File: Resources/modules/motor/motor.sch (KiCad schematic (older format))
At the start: 15 parts, among them J1 power, J2 from switches, J3 motor, J4 towards uC, U1 L293D

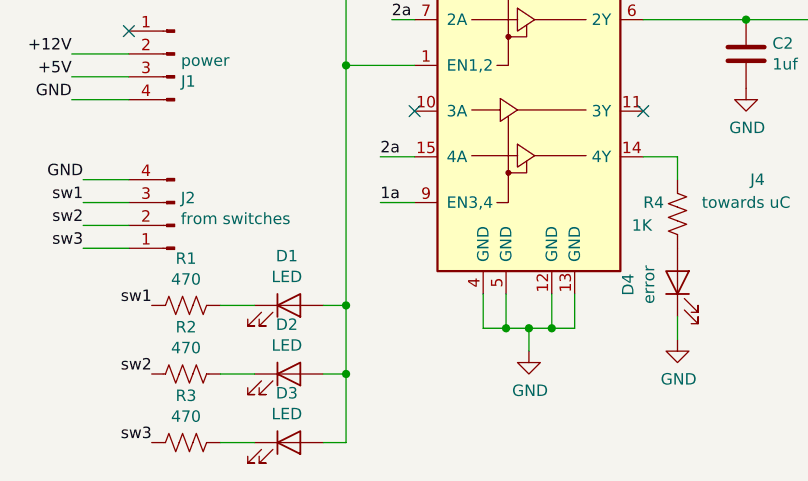
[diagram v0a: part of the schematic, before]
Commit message: Motor module: grounded 'EN3,4'; terminal connector footprint corrected; 'error led' changed to 3mm; proper footprints for 'switches' and 'towards uC' connectors; proper labelling; added 'designed using Kicad' symbol
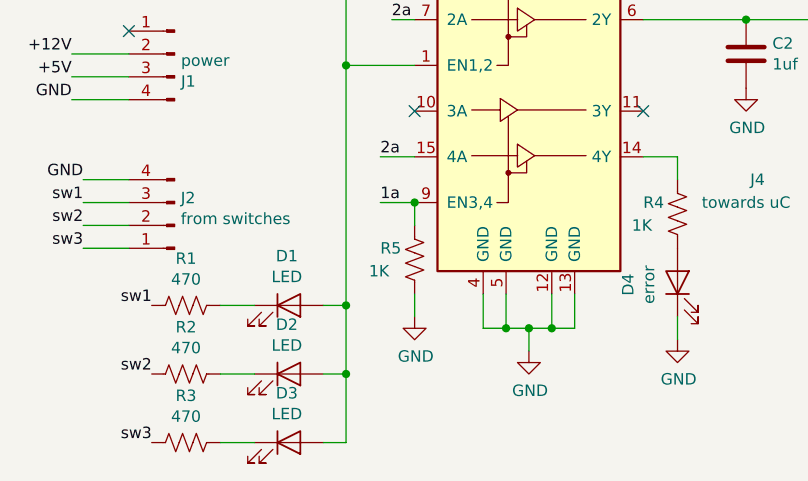
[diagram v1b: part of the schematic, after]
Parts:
- added R5: 1K, Resistor_THT:R_Axial_DIN0207_L6.3mm_D2.5mm_P5.08mm_Vertical, symbol Device:R_US
- C1, C2: footprint Capacitors_THT:C_Disc_D3.8mm_W2.6mm_P2.50mm -> Capacitor_THT:C_Disc_D3.8mm_W2.6mm_P2.50mm
- D1, D2, D3: footprint LEDs:LED_D3.0mm -> LED_THT:LED_D3.0mm
- D4: footprint LEDs:LED_D5.0mm -> LED_THT:LED_D3.0mm
- J1: footprint Connectors_JST:JST_EH_B04B-EH-A_04x2.50mm_Straight -> Connector_JST:JST_EH_B4B-EH-A_1x04_P2.50mm_Vertical
- J2: footprint Connectors_JST:JST_EH_B04B-EH-A_04x2.50mm_Straight -> Connector_PinHeader_2.54mm:PinHeader_1x04_P2.54mm_Vertical
- J3: footprint TerminalBlocks_Phoenix:TerminalBlock_Phoenix_MPT-2.54mm_2pol -> TerminalBlock_Phoenix:TerminalBlock_Phoenix_MKDS-1,5-2_1x02_P5.00mm_Horizontal
- J4: footprint Connectors_JST:JST_EH_B05B-EH-A_05x2.50mm_Straight -> Connector_PinHeader_2.54mm:PinHeader_1x05_P2.54mm_Vertical
- R1, R2, R3, R4: footprint Resistors_THT:R_Axial_DIN0207_L6.3mm_D2.5mm_P5.08mm_Vertical -> Resistor_THT:R_Axial_DIN0207_L6.3mm_D2.5mm_P5.08mm_Vertical
- U1: footprint Housings_DIP:DIP-16_W7.62mm_Socket_LongPads -> Package_DIP:DIP-16_W7.62mm_Socket_LongPads
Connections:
- net 1a: now also R5.1
- net GND: now also R5.2
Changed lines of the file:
@@
 EESchema Schematic File Version 4
 LIBS:motor-cache
-EELAYER 26 0
+EELAYER 30 0
 EELAYER END
 $Descr A4 11693 8268
@@
 F 0 "J3" V 7223 3330 50  0000 L CNN
 F 1 "motor" H 7450 3200 50  0000 L CNN
-F 2 "TerminalBlocks_Phoenix:TerminalBlock_Phoenix_MPT-2.54mm_2pol" H 7350 3250 50  0001 C CNN
+F 2 "TerminalBlock_Phoenix:TerminalBlock_Phoenix_MKDS-1,5-2_1x02_P5.00mm_Horizontal" H 7350 3250 50  0001 C CNN
 F 3 "~" H 7350 3250 50  0001 C CNN
 	1    7350 3250
@@
 F 0 "U1" H 6150 4850 50  0000 C CNN
 F 1 "L293D" H 6150 4750 50  0000 C CNN
-F 2 "Housings_DIP:DIP-16_W7.62mm_Socket_LongPads" H 5800 3050 50  0001 L CNN
+F 2 "Package_DIP:DIP-16_W7.62mm_Socket_LongPads" H 5800 3050 50  0001 L CNN
 F 3 "http://www.ti.com/lit/ds/symlink/l293.pdf" H 5250 4500 50  0001 C CNN
 	1    5550 3800
@@
 F 0 "J4" H 6550 4300 50  0000 C CNN
 F 1 "towards uC" H 6500 4200 50  0000 C CNN
-F 2 "Connectors_JST:JST_EH_B05B-EH-A_05x2.50mm_Straight" H 6900 4200 50  0001 C CNN
+F 2 "Connector_PinHeader_2.54mm:PinHeader_1x05_P2.54mm_Vertical" H 6900 4200 50  0001 C CNN
 F 3 "~" H 6900 4200 50  0001 C CNN
 	1    6900 4200
@@
 F 0 "J1" H 3972 3430 50  0000 R CNN
 F 1 "power" H 3972 3521 50  0000 R CNN
-F 2 "Connectors_JST:JST_EH_B04B-EH-A_04x2.50mm_Straight" H 4000 3550 50  0001 C CNN
+F 2 "Connector_JST:JST_EH_B4B-EH-A_1x04_P2.50mm_Vertical" H 4000 3550 50  0001 C CNN
 F 3 "~" H 4000 3550 50  0001 C CNN
 	1    4000 3550
@@
 F 0 "J2" H 3973 4180 50  0000 R CNN
 F 1 "from switches" H 3973 4271 50  0000 R CNN
-F 2 "Connectors_JST:JST_EH_B04B-EH-A_04x2.50mm_Straight" H 4000 4300 50  0001 C CNN
+F 2 "Connector_PinHeader_2.54mm:PinHeader_1x04_P2.54mm_Vertical" H 4000 4300 50  0001 C CNN
 F 3 "~" H 4000 4300 50  0001 C CNN
 	1    4000 4300
@@
 F 0 "C2" H 6615 3596 50  0000 L CNN
 F 1 "1uf" H 6615 3505 50  0000 L CNN
-F 2 "Capacitors_THT:C_Disc_D3.8mm_W2.6mm_P2.50mm" H 6538 3400 50  0001 C CNN
+F 2 "Capacitor_THT:C_Disc_D3.8mm_W2.6mm_P2.50mm" H 6538 3400 50  0001 C CNN
 F 3 "~" H 6500 3550 50  0001 C CNN
 	1    6500 3550
@@
 F 0 "C1" H 6615 3096 50  0000 L CNN
 F 1 "1uf" H 6615 3005 50  0000 L CNN
-F 2 "Capacitors_THT:C_Disc_D3.8mm_W2.6mm_P2.50mm" H 6538 2900 50  0001 C CNN
+F 2 "Capacitor_THT:C_Disc_D3.8mm_W2.6mm_P2.50mm" H 6538 2900 50  0001 C CNN
 F 3 "~" H 6500 3050 50  0001 C CNN
 	1    6500 3050
@@
 F 0 "D1" H 4491 4866 50  0000 C CNN
 F 1 "LED" H 4491 4775 50  0000 C CNN
-F 2 "LEDs:LED_D3.0mm" H 4500 4650 50  0001 C CNN
+F 2 "LED_THT:LED_D3.0mm" H 4500 4650 50  0001 C CNN
 F 3 "~" H 4500 4650 50  0001 C CNN
 	1    4500 4650
@@
 F 0 "D2" H 4491 5166 50  0000 C CNN
 F 1 "LED" H 4491 5075 50  0000 C CNN
-F 2 "LEDs:LED_D3.0mm" H 4500 4950 50  0001 C CNN
+F 2 "LED_THT:LED_D3.0mm" H 4500 4950 50  0001 C CNN
 F 3 "~" H 4500 4950 50  0001 C CNN
 	1    4500 4950
@@
 F 0 "D3" H 4491 5466 50  0000 C CNN
 F 1 "LED" H 4491 5375 50  0000 C CNN
-F 2 "LEDs:LED_D3.0mm" H 4500 5250 50  0001 C CNN
+F 2 "LED_THT:LED_D3.0mm" H 4500 5250 50  0001 C CNN
 F 3 "~" H 4500 5250 50  0001 C CNN
 	1    4500 5250
@@
 F 0 "R1" V 4255 4650 50  0000 C CNN
 F 1 "470" V 4164 4650 50  0000 C CNN
-F 2 "Resistors_THT:R_Axial_DIN0207_L6.3mm_D2.5mm_P5.08mm_Vertical" V 4090 4640 50  0001 C CNN
+F 2 "Resistor_THT:R_Axial_DIN0207_L6.3mm_D2.5mm_P5.08mm_Vertical" V 4090 4640 50  0001 C CNN
 F 3 "~" H 4050 4650 50  0001 C CNN
 	1    4050 4650
@@
 F 0 "R2" V 4255 4950 50  0000 C CNN
 F 1 "470" V 4164 4950 50  0000 C CNN
-F 2 "Resistors_THT:R_Axial_DIN0207_L6.3mm_D2.5mm_P5.08mm_Vertical" V 4090 4940 50  0001 C CNN
+F 2 "Resistor_THT:R_Axial_DIN0207_L6.3mm_D2.5mm_P5.08mm_Vertical" V 4090 4940 50  0001 C CNN
 F 3 "~" H 4050 4950 50  0001 C CNN
 	1    4050 4950
@@
 F 0 "R3" V 4255 5250 50  0000 C CNN
 F 1 "470" V 4164 5250 50  0000 C CNN
-F 2 "Resistors_THT:R_Axial_DIN0207_L6.3mm_D2.5mm_P5.08mm_Vertical" V 4090 5240 50  0001 C CNN
+F 2 "Resistor_THT:R_Axial_DIN0207_L6.3mm_D2.5mm_P5.08mm_Vertical" V 4090 5240 50  0001 C CNN
 F 3 "~" H 4050 5250 50  0001 C CNN
 	1    4050 5250
@@
 F 0 "R4" H 6050 4300 50  0000 L CNN
 F 1 "1K" H 6000 4200 50  0000 L CNN
-F 2 "Resistors_THT:R_Axial_DIN0207_L6.3mm_D2.5mm_P5.08mm_Vertical" V 6240 4240 50  0001 C CNN
+F 2 "Resistor_THT:R_Axial_DIN0207_L6.3mm_D2.5mm_P5.08mm_Vertical" V 6240 4240 50  0001 C CNN
 F 3 "~" H 6200 4250 50  0001 C CNN
 	1    6200 4250
@@
 F 0 "D4" H 6191 4766 50  0000 C CNN
 F 1 "error" H 6191 4675 50  0000 C CNN
-F 2 "LEDs:LED_D5.0mm" H 6200 4550 50  0001 C CNN
+F 2 "LED_THT:LED_D3.0mm" H 6200 4550 50  0001 C CNN
 F 3 "~" H 6200 4550 50  0001 C CNN
 	1    6200 4550
@@
 	3800 3750 3550 3750
 NoConn ~ 3800 3450
+$Comp
+L Device:R_US R5
+U 1 1 5D5EA8A2
+P 5050 4450
+F 0 "R5" H 4900 4500 50  0000 L CNN
+F 1 "1K" H 4850 4400 50  0000 L CNN
+F 2 "Resistor_THT:R_Axial_DIN0207_L6.3mm_D2.5mm_P5.08mm_Vertical" V 5090 4440 50  0001 C CNN
+F 3 "~" H 5050 4450 50  0001 C CNN
+	1    5050 4450
+	1    0    0    -1
+$EndComp
+Wire Wire Line
+	5050 4300 5050 4200
+Connection ~ 5050 4200
+$Comp
+L power:GND #PWR0107
+U 1 1 5D5EBDE4
+P 5050 4700
+F 0 "#PWR0107" H 5050 4450 50  0001 C CNN
+F 1 "GND" H 5055 4527 50  0000 C CNN
+F 2 "" H 5050 4700 50  0001 C CNN
+F 3 "" H 5050 4700 50  0001 C CNN
+	1    5050 4700
+	1    0    0    -1
+$EndComp
+Wire Wire Line
+	5050 4600 5050 4700
 $EndSCHEMATC
